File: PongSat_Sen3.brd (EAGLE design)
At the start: 39.1 x 39.2 mm, 30 parts, among them U1 MIC5129 3v3, U2 Micro SD, X1 USB-MICROB, Y1 8MHz

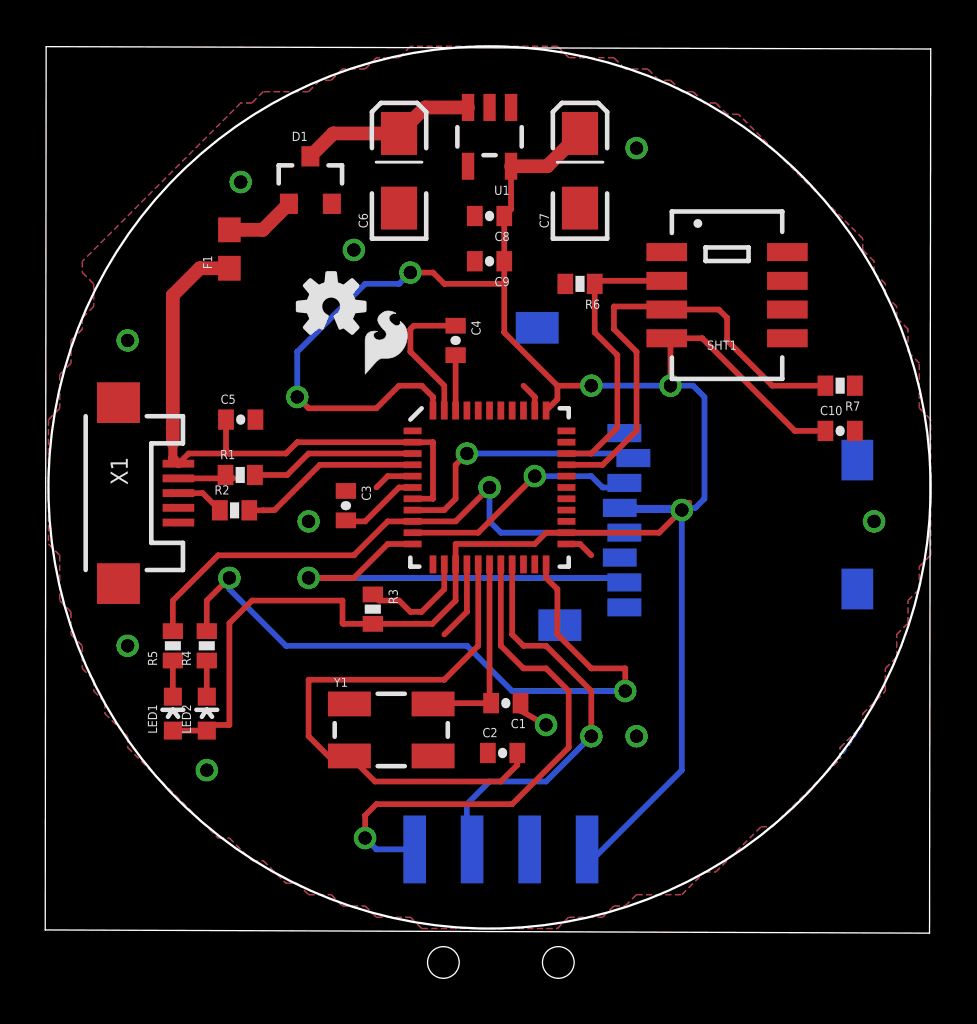
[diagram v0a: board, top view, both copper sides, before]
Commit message: Updated PCB
Completed PCB (V3 BETA) uploaded. PCB is now produceable, but not ERC'd
or DRC'd.
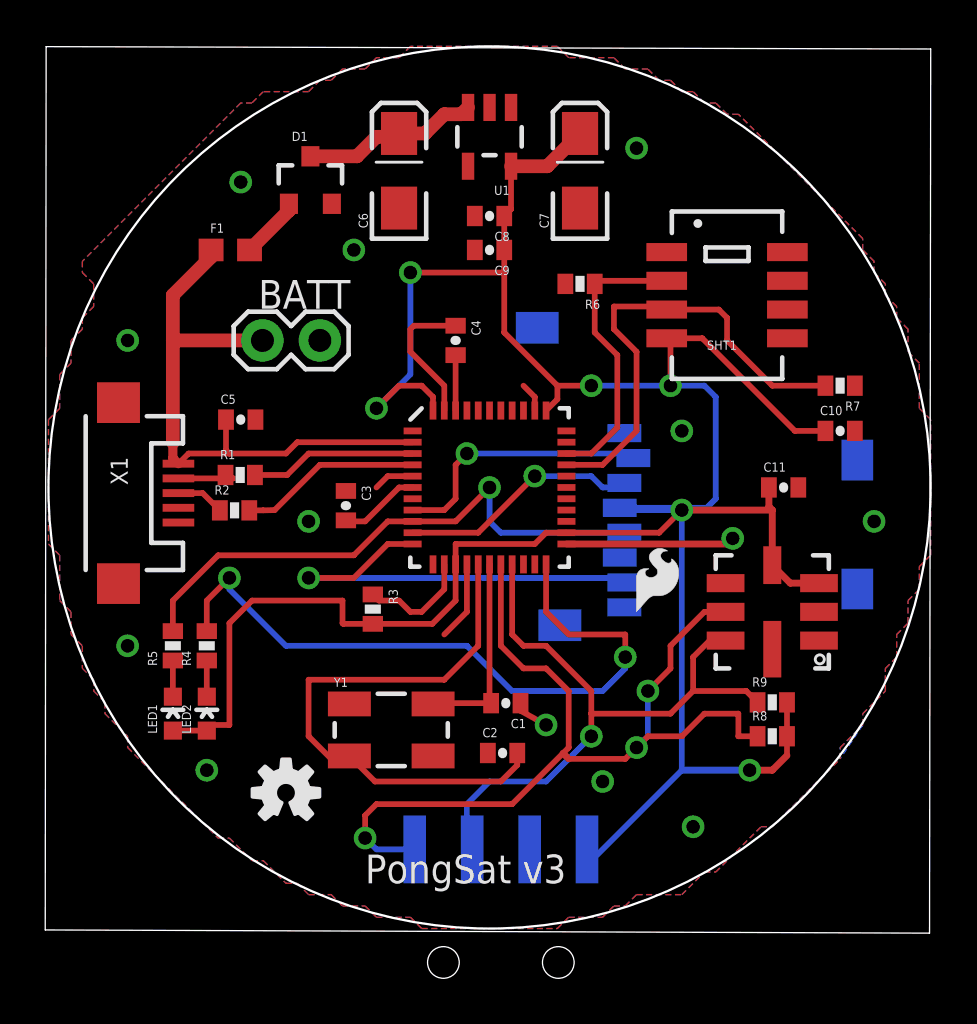
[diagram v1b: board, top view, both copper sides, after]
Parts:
- added BATT: (no value), SparkFun-Connectors:1X02
- added C11: 100nF, SparkFun-Passives:0402-CAP
- added R8, R9: 4.7K, SparkFun-Passives:0402-RES
- added U$3: BMP085, SparkFun-Sensors:BMP085
- moved U$1 21.6 mm to (10.5, 6.00)
- moved U$2 15.9 mm to (26.0, 14.0)
- moved C9 0.50 mm to (19.5, 30.0)
- moved F1 0.06 mm to (8.04, 30.0), turned to 0 degrees
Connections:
- new net EOC: U$3.2
- new net XCLR: U$3.8
- net 3.3V: now also C11.1, R8.2, R9.2, U$3.3, U$3.4
- net GND: now also BATT.1, C11.2, U$3.1
- net SCL: now also R8.1, U$3.6
- net SDA: now also R9.1, U$3.7
- net UVCC: now also BATT.2
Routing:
- net SCL: track 23.8 -> 42.5 mm, vias 1 -> 3
- net 3.3V: track 114.9 -> 126.9 mm, vias 5 -> 6
- net SDA: track 18.5 -> 29.7 mm
- net GND: track 15.8 -> 22.0 mm, vias 10 -> 13
- net UVCC: track 27.2 -> 26.5 mm
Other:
- board text added: "PongSat v3"

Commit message: PCB Update
Updated PCB with SD fix and also added new Schematics to repo.
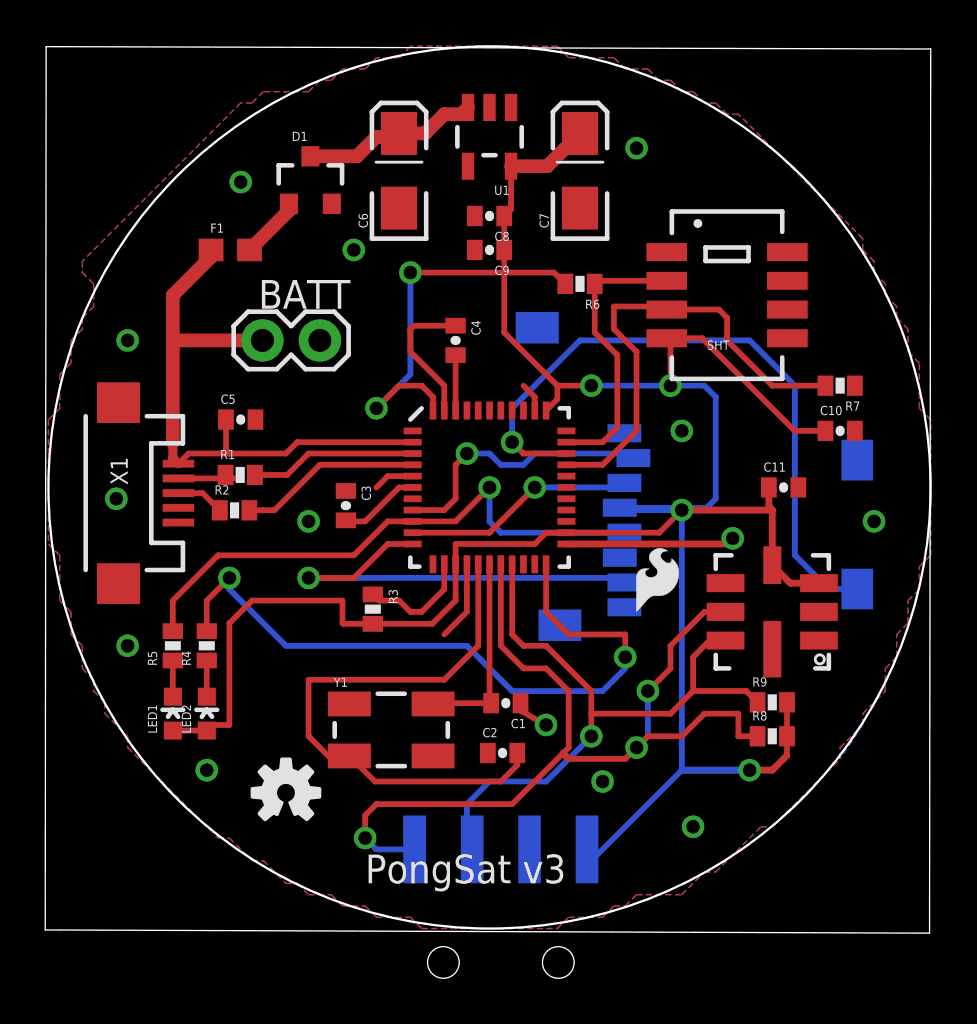
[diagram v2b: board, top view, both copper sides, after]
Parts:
- renumbered SHT1 to SHT, U$3 to BMP
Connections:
- net CD: now also 32U4.31
- net HTDAT: now also 32U4.32; no longer 32U4.31
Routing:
- net CD: track 0.00 -> 29.6 mm, vias 0 -> 1
- net 3.3V: track 126.9 -> 129.8 mm
- net GND: vias 13 -> 14
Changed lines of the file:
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@@
 <element name="C6" library="SparkFun-Passives" package="EIA3216-KIT" value="10uF" x="15.5" y="33.5" locked="yes" rot="R90"/>
 <element name="D1" library="SparkFun-DiscreteSemi" package="SOT23-3" value="" x="11.58" y="33.04" locked="yes"/>
-<element name="F1" library="SparkFun-PowerIC" package="0603" value="PTC0603" x="8.04" y="30"/>
+<element name="F1" library="SparkFun-PowerIC" package="0603" value="PTC0603" x="8.04" y="30" locked="yes"/>
 <element name="C7" library="SparkFun-Passives" package="EIA3216-KIT" value="10uF" x="23.5" y="33.5" locked="yes" rot="R90"/>
 <element name="C8" library="SparkFun-Passives" package="0402-CAP" value="1uF" x="19.5" y="31.5" locked="yes" rot="R180"/>
@@
 <element name="U$1" library="SparkFun-Aesthetics" package="OSHW-LOGO-S" value="" x="10.5" y="6"/>
 <element name="U$2" library="SparkFun-Aesthetics" package="SFE-LOGO-FLAME" value="" x="26" y="14"/>
-<element name="SHT1" library="SparkFun-Sensors" package="SHT1X" value="SHT1XSMD" x="30" y="28" locked="yes"/>
+<element name="SHT" library="SparkFun-Sensors" package="SHT1X" value="SHT1XSMD" x="30" y="28" locked="yes"/>
 <element name="C10" library="SparkFun-Passives" package="0402-CAP" value="0.1uF" x="35" y="22"/>
 <element name="R6" library="SparkFun-Passives" package="0402-RES" value="10K" x="23.5" y="28.5" rot="R180"/>
 <element name="R7" library="SparkFun-Passives" package="0402-RES" value="10K" x="35" y="24" rot="R180"/>
-<element name="U$3" library="SparkFun-Sensors" package="BMP085" value="BMP085" x="32" y="14" locked="yes" rot="R180"/>
+<element name="BMP" library="SparkFun-Sensors" package="BMP085" value="BMP085" x="32" y="14" locked="yes" rot="R180"/>
 <element name="R8" library="SparkFun-Passives" package="0402-RES" value="4.7K" x="32" y="8.5"/>
 <element name="R9" library="SparkFun-Passives" package="0402-RES" value="4.7K" x="32" y="10"/>
 <element name="C11" library="SparkFun-Passives" package="0402-CAP" value="100nF" x="32.5" y="19.5"/>
-<element name="BATT" library="SparkFun-Connectors" package="1X02" value="" x="12" y="26" smashed="yes" rot="R180">
+<element name="BATT" library="SparkFun-Connectors" package="1X02" value="" x="12" y="26" locked="yes" smashed="yes" rot="R180">
 <attribute name="NAME" x="13.3462" y="28.6712" size="1.27" layer="25" ratio="10" rot="R180"/>
 <attribute name="VALUE" x="13.27" y="29.175" size="1.27" layer="27" rot="R180"/>
@@
 <via x="3.5" y="12.5" extent="1-16" drill="0.6"/>
 <via x="28.5" y="4.5" extent="1-16" drill="0.6"/>
-<contactref element="SHT1" pad="1"/>
-<contactref element="SHT1" pad="1"/>
+<contactref element="SHT" pad="1"/>
+<contactref element="SHT" pad="1"/>
 <via x="11.5" y="18" extent="1-16" drill="0.6"/>
 <contactref element="C10" pad="2"/>
 <contactref element="R7" pad="1"/>
-<contactref element="U$3" pad="1"/>
-<contactref element="U$3" pad="1"/>
+<contactref element="BMP" pad="1"/>
+<contactref element="BMP" pad="1"/>
 <via x="30.25" y="17.25" extent="1-16" drill="0.6"/>
 <wire x1="22.9" y1="17" x2="30" y2="17" width="0.3048" layer="1"/>
@@
 <via x="28" y="22" extent="1-16" drill="0.6"/>
 <contactref element="BATT" pad="1"/>
+<via x="3" y="19" extent="1-16" drill="0.6"/>
 </signal>
 <signal name="N$3">
@@
 <contactref element="32U4" pad="10"/>
 <contactref element="U2" pad="3"/>
-<wire x1="16.1" y1="17.5" x2="19" y2="17.5" width="0.254" layer="1"/>
-<wire x1="19" y1="17.5" x2="21.5" y2="20" width="0.254" layer="1"/>
-<via x="21.5" y="20" extent="1-16" drill="0.6"/>
-<wire x1="21.5" y1="20" x2="24" y2="20" width="0.254" layer="16"/>
-<wire x1="24" y1="20" x2="24.5" y2="19.5" width="0.254" layer="16"/>
-<wire x1="24.5" y1="19.5" x2="25.26" y2="19.5" width="0.254" layer="16"/>
+<wire x1="16.1" y1="17.5" x2="19.5" y2="17.5" width="0.254" layer="1"/>
+<wire x1="19.5" y1="17.5" x2="21.5" y2="19.5" width="0.254" layer="1"/>
+<via x="21.5" y="19.5" extent="1-16" drill="0.6"/>
+<wire x1="21.5" y1="19.5" x2="25.26" y2="19.5" width="0.254" layer="16"/>
 <wire x1="25.26" y1="19.5" x2="25.46" y2="19.7" width="0.254" layer="16"/>
 </signal>
@@
 <wire x1="18.5" y1="5.5" x2="18.5" y2="3.73" width="0.254" layer="16"/>
 <wire x1="18.5" y1="3.73" x2="18.73" y2="3.5" width="0.254" layer="16"/>
-<contactref element="U$3" pad="7"/>
+<contactref element="BMP" pad="7"/>
 <wire x1="29.935" y1="12.73" x2="29.23" y2="12.73" width="0.254" layer="1"/>
 <wire x1="29.23" y1="12.73" x2="28.5" y2="12" width="0.254" layer="1"/>
@@
 <wire x1="23" y1="10.5" x2="23" y2="8" width="0.254" layer="1"/>
 <wire x1="16" y1="3.69" x2="16.19" y2="3.5" width="0.254" layer="16"/>
-<contactref element="U$3" pad="6"/>
+<contactref element="BMP" pad="6"/>
 <wire x1="29.935" y1="14" x2="29" y2="14" width="0.254" layer="1"/>
 <wire x1="29" y1="14" x2="27.5" y2="12.5" width="0.254" layer="1"/>
@@
 <wire x1="8" y1="9" x2="7.25" y2="9" width="0.254" layer="1"/>
 <wire x1="7.25" y1="9" x2="7" y2="8.75" width="0.254" layer="1"/>
-<contactref element="SHT1" pad="4"/>
+<contactref element="SHT" pad="4"/>
 <contactref element="C10" pad="1"/>
 <contactref element="R6" pad="2"/>
@@
 <wire x1="27.5" y1="26.095" x2="27.5" y2="24" width="0.254" layer="1"/>
 <via x="27.5" y="24" extent="1-16" drill="0.6"/>
-<contactref element="U$3" pad="3"/>
-<contactref element="U$3" pad="4"/>
+<contactref element="BMP" pad="3"/>
+<contactref element="BMP" pad="4"/>
 <wire x1="34.065" y1="15.27" x2="32.795" y2="15.27" width="0.3048" layer="1"/>
 <wire x1="32.795" y1="15.27" x2="32" y2="16.065" width="0.3048" layer="1"/>
@@
 <wire x1="16" y1="29" x2="16" y2="24.5" width="0.254" layer="16"/>
 <wire x1="16" y1="24.5" x2="14.5" y2="23" width="0.254" layer="16"/>
-<wire x1="20.15" y1="29" x2="22.85" y2="28.5" width="0" layer="19" extent="1-1"/>
+<wire x1="22.85" y1="28.5" x2="22.35" y2="29" width="0.254" layer="1"/>
+<wire x1="22.35" y1="29" x2="20.15" y2="29" width="0.254" layer="1"/>
 </signal>
 <signal name="CS">
@@
 <wire x1="18" y1="20.5" x2="18.5" y2="21" width="0.254" layer="1"/>
 <via x="18.5" y="21" extent="1-16" drill="0.6"/>
-<wire x1="18.5" y1="21" x2="25.66" y2="21" width="0.254" layer="16"/>
+<wire x1="18.5" y1="21" x2="19.5" y2="21" width="0.254" layer="16"/>
+<wire x1="19.5" y1="21" x2="20" y2="20.5" width="0.254" layer="16"/>
+<wire x1="20" y1="20.5" x2="21" y2="20.5" width="0.254" layer="16"/>
+<wire x1="21" y1="20.5" x2="21.5" y2="21" width="0.254" layer="16"/>
+<wire x1="21.5" y1="21" x2="25.66" y2="21" width="0.254" layer="16"/>
 <wire x1="25.66" y1="21" x2="25.86" y2="20.8" width="0.254" layer="16"/>
 </signal>
@@
 <signal name="CD">
 <contactref element="U2" pad="CD1"/>
+<contactref element="32U4" pad="31"/>
+<wire x1="22.9" y1="21" x2="21" y2="21" width="0.254" layer="1"/>
+<wire x1="21" y1="21" x2="20.5" y2="21.5" width="0.254" layer="1"/>
+<via x="20.5" y="21.5" extent="1-16" drill="0.6"/>
+<wire x1="35.76" y1="15.01" x2="34.49" y2="15.01" width="0.254" layer="16"/>
+<wire x1="34.49" y1="15.01" x2="33" y2="16.5" width="0.254" layer="16"/>
+<wire x1="33" y1="16.5" x2="33" y2="24" width="0.254" layer="16"/>
+<wire x1="33" y1="24" x2="31" y2="26" width="0.254" layer="16"/>
+<wire x1="31" y1="26" x2="23.5" y2="26" width="0.254" layer="16"/>
+<wire x1="23.5" y1="26" x2="20.5" y2="23" width="0.254" layer="16"/>
+<wire x1="20.5" y1="23" x2="20.5" y2="21.5" width="0.254" layer="16"/>
 </signal>
 <signal name="HTCK">
-<contactref element="SHT1" pad="3"/>
+<contactref element="SHT" pad="3"/>
 <contactref element="R7" pad="2"/>
 <contactref element="32U4" pad="30"/>
@@
 </signal>
 <signal name="HTDAT">
-<contactref element="SHT1" pad="2"/>
+<contactref element="SHT" pad="2"/>
 <contactref element="R6" pad="1"/>
-<contactref element="32U4" pad="31"/>
-<wire x1="25.15" y1="22.15" x2="24" y2="21" width="0.254" layer="1"/>
-<wire x1="24" y1="21" x2="22.9" y2="21" width="0.254" layer="1"/>
 <wire x1="27.333" y1="28.635" x2="24.285" y2="28.635" width="0.254" layer="1"/>
 <wire x1="24.285" y1="28.635" x2="24.15" y2="28.5" width="0.254" layer="1"/>
@@
 <wire x1="24.15" y1="26.35" x2="25.15" y2="25.35" width="0.254" layer="1"/>
 <wire x1="25.15" y1="25.35" x2="25.15" y2="22.15" width="0.254" layer="1"/>
+<contactref element="32U4" pad="32"/>
+<wire x1="22.9" y1="21.5" x2="24.5" y2="21.5" width="0.254" layer="1"/>
+<wire x1="24.5" y1="21.5" x2="25.15" y2="22.15" width="0.254" layer="1"/>
 </signal>
 <signal name="EOC">
-<contactref element="U$3" pad="2"/>
+<contactref element="BMP" pad="2"/>
 </signal>
 <signal name="XCLR">
-<contactref element="U$3" pad="8"/>
+<contactref element="BMP" pad="8"/>
 </signal>
 </signals>

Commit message: Updated PCB V3 Rev 3
Updated PCB with new Silkscreen, improved routing and placement, bias
and mounting holes. Included Schematics, PCB Printouts and Assembly
diagrams in repo :-)
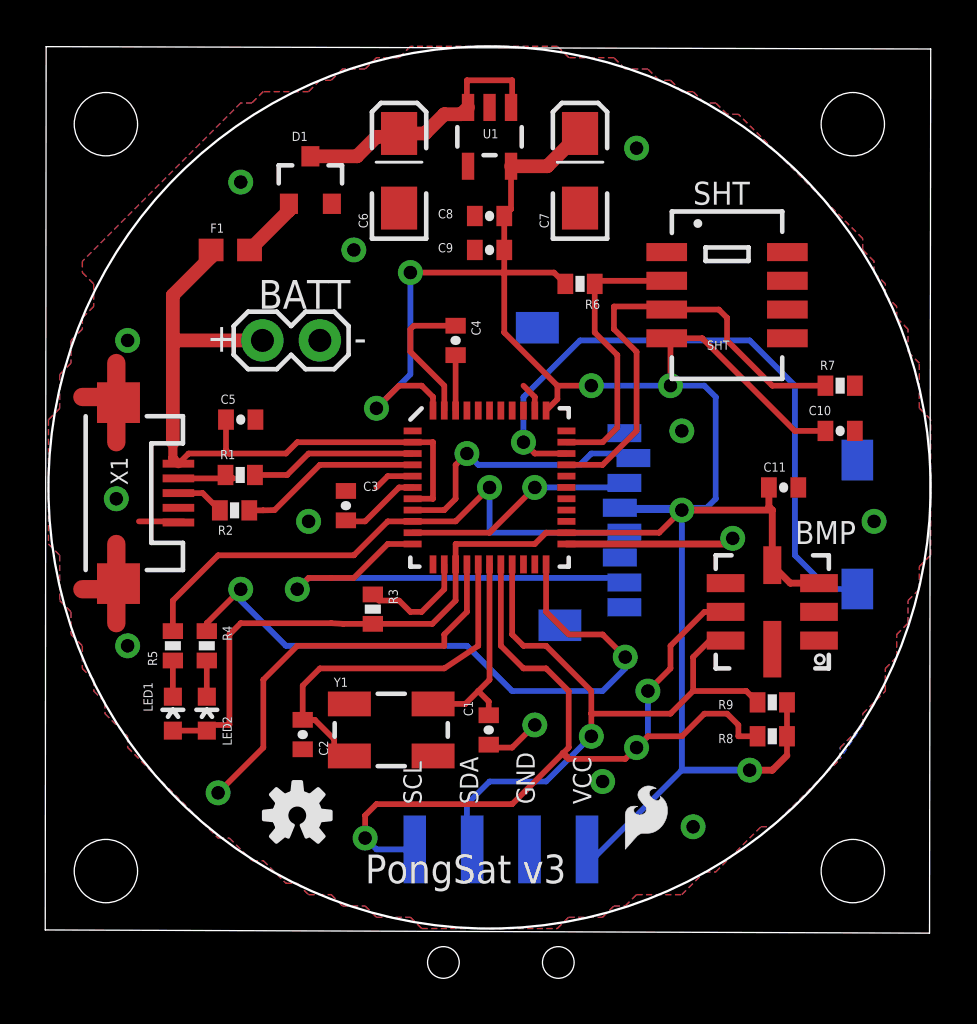
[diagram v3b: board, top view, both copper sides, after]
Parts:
- BATT: value (none) -> ~6V
- I2C: value (none) -> 3.3V
- moved U$2 10.5 mm to (25.5, 3.50)
- moved C2 8.87 mm to (11.2, 8.58), turned to 90 degrees
- moved C1 1.40 mm to (19.5, 8.78), turned to 90 degrees
- moved U$1 1.12 mm to (11.0, 5.00)
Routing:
- net GND: track 22.0 -> 49.2 mm
- net N$1: track 25.2 -> 17.0 mm
- net RAW: track 7.86 -> 12.3 mm
- net UVCC: track 26.5 -> 30.8 mm
- net 3.3V: track 129.8 -> 128.1 mm
- net TXLED: track 30.6 -> 29.0 mm
- net MISO: track 19.3 -> 20.7 mm
- net N$2: track 8.75 -> 9.46 mm
- net CD: track 29.6 -> 28.8 mm
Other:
- board text added: "+"
- board text added: "-"
- board text added: "BMP"
- board text added: "GND"
- board text added: "SCL"
- board text added: "SDA"
- board text added: "SHT"
- board text added: "VCC"
